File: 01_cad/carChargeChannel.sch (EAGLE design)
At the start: 100 parts, among them IC1 LT1513, IC3 PIC18F2420, T1 BC847A, T2 IRL530, X2 2X3

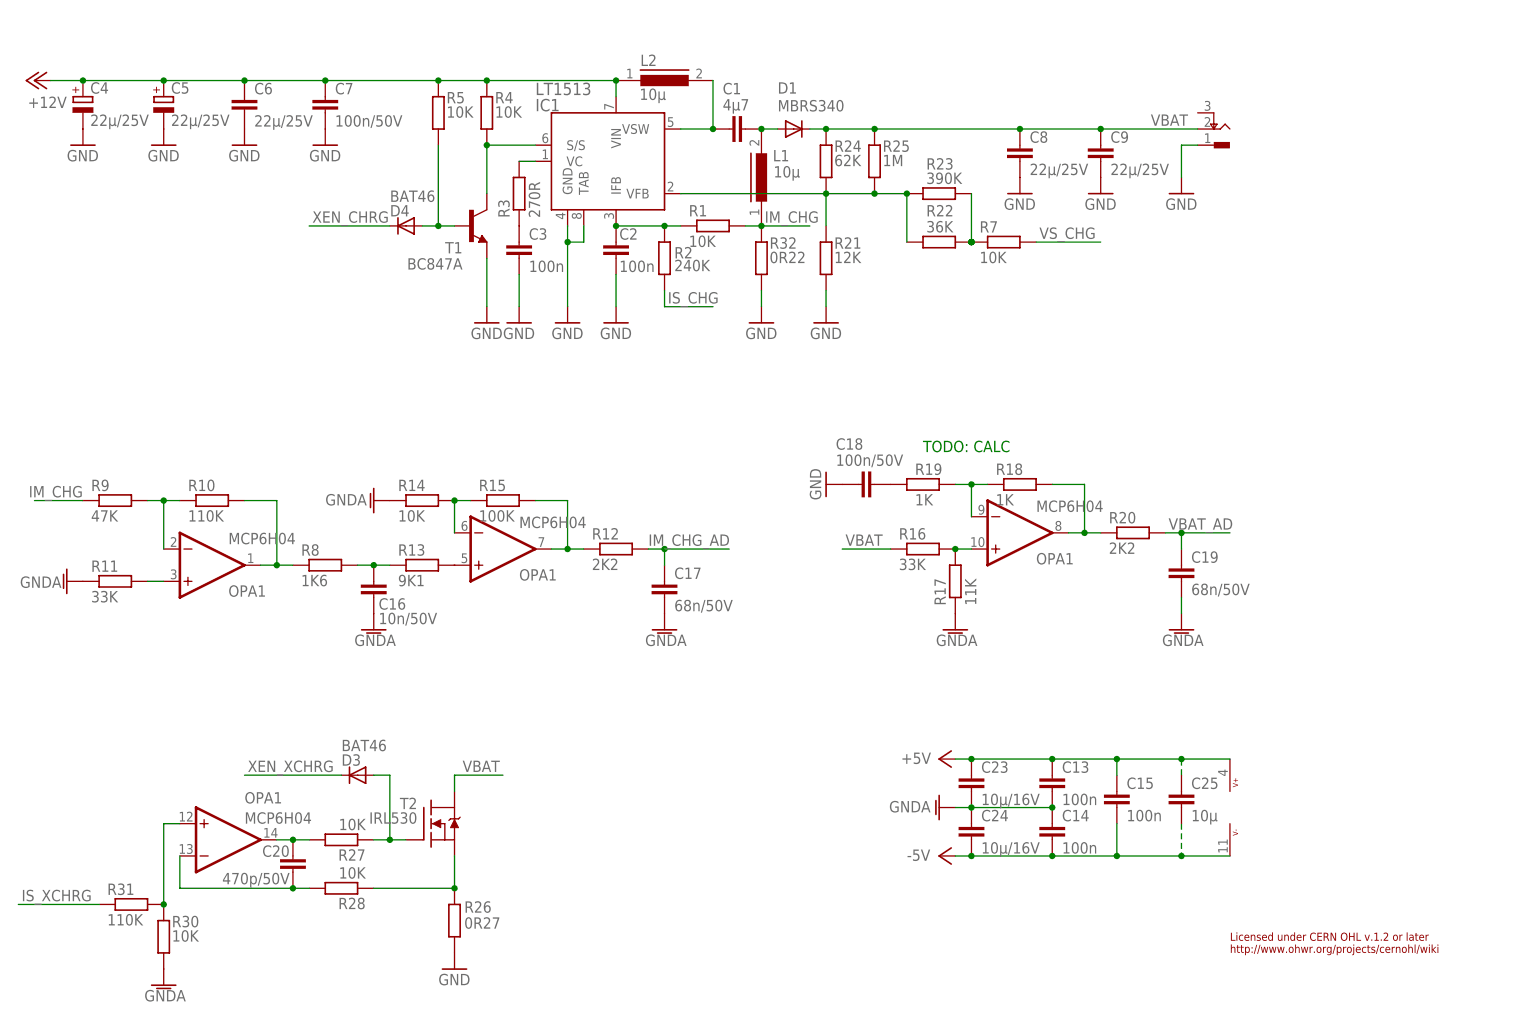
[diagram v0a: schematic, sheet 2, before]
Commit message: add TPS60403 for pwr supply
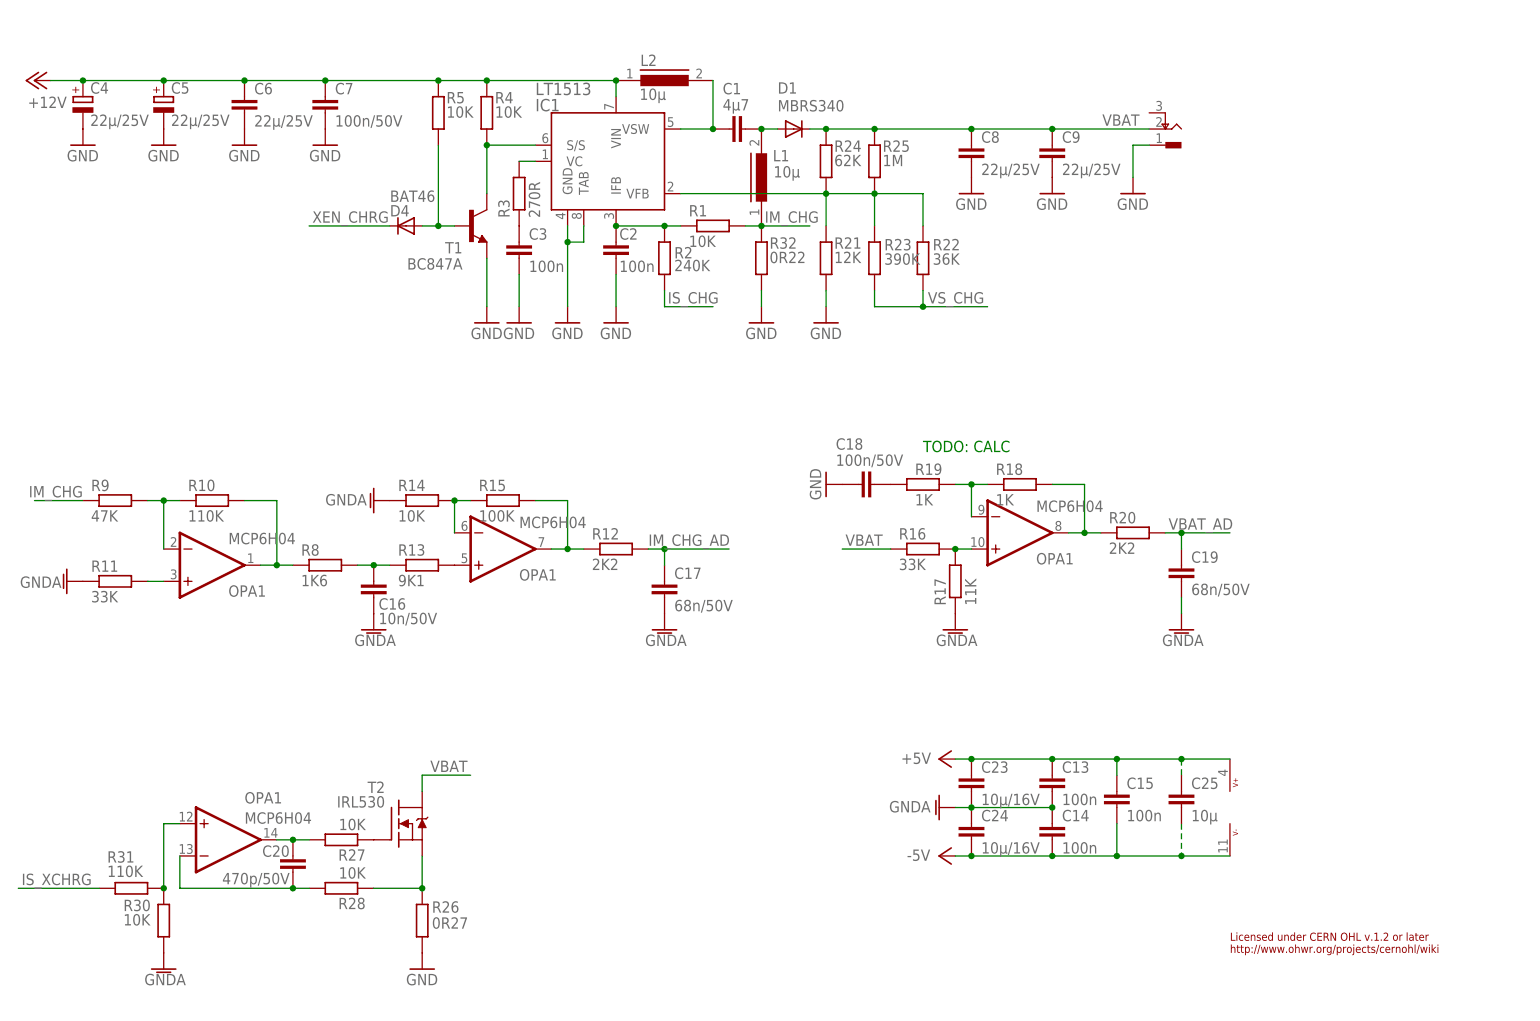
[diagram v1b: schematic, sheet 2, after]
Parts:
- removed D3: BAT46, omcDiode:BAT46W
- removed R7: 10K, omcResistor:R1206-10000-1%
- added IC2: PIC18F2420, omcPIC:PIC18F2420/SO
- IC3: value PIC18F2420 -> TPS60403; device omcPIC:PIC18F2420/SO -> omcPwrSupply:TPS60403DBVT
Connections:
- removed net LED1: IC3.5@RC
- removed net N$28: R22.1, R23.1, R7.1
- removed net XEN_XCHRG: D3.C, IC3.4@RB
- net !CS_DAC1: now also IC2.0@RB; no longer IC3.0@RB
- net !CS_DAC2: now also IC2.1@RB; no longer IC3.1@RB
- net !MCLR: now also IC2.!MCLR; no longer IC3.!MCLR
- net GND: now also IC2.VSS@VSS0, IC2.VSS@VSS1; no longer IC3.VSS@VSS0, IC3.VSS@VSS1
- net GNDA: now also IC2.4@RA; no longer IC3.4@RA
- net IM_CHG_AD: now also IC2.0@RA; no longer IC3.0@RA
- net LED2: now also IC2.5@RB; no longer IC3.5@RB
- net N$10: now also IC2.1@RC; no longer IC3.1@RC
- net N$20: now also IC2.0@RC; no longer IC3.0@RC
- net N$23: no longer D3.A
- net N$30: now also IC2.2@RC; no longer IC3.2@RC
- net N$34: now also IC2.OSC@1; no longer IC3.OSC@1
- net N$35: now also IC2.OSC@2; no longer IC3.OSC@2
- net PGC: now also IC2.6@RB; no longer IC3.6@RB
- net PGD: now also IC2.7@RB; no longer IC3.7@RB
- net PWRGD: now also IC2.2@RB; no longer IC3.2@RB
- net RXD: now also IC2.6@RC; no longer IC3.6@RC
- net SCL: now also IC2.3@RC; no longer IC3.3@RC
- net SDA: now also IC2.4@RC; no longer IC3.4@RC
- net TXD: now also IC2.7@RC; no longer IC3.7@RC
- net VBAT_AD: now also IC2.1@RA; no longer IC3.1@RA
- net VDD: now also IC2.VDD; no longer IC3.VDD
- net VREF_ADC: now also IC2.5@RA; no longer IC3.5@RA
- net VS_CHG: now also R22.1, R23.1; no longer R7.2
- net XEN_CHRG: now also IC2.3@RB; no longer IC3.3@RB
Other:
- note removed: "( 36k || 390k ) = 32.96k"
- moved on the sheet: C8, C9, R22, R23, R26, R30, R31, T2

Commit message: intermediate
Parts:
- removed C21, C36, C38, C39, C40: 47µ/6V, omcCapacitor:X5R-47000000P-1206
- removed C37, C41: 47µ/16V, omcCapacitor:X5R-47000000P-1210
- removed L3: 100µ, omcInductor:LQH3C101K
- removed R34: 0R, omcResistor:R1206-0.0-1%
- added C42, C43, C44: 1µ/50V, omcCapacitor:X7R-1000000P-1206
- added C45: 10µ/16V, omcCapacitor:X7R-10000000P-1206
- added C46: 47µ/16V, omcCapacitor:AEC-47U-16V-C
- added C47: 100n/50V, omcCapacitor:X7R-100000P-1206
- added C48: 22µ/16V, omcCapacitor:AEC-22U-16V-B
- added F1: T 1A0, omcFuse:OMT-T1A0-125V
- added IC4: 7805, omcPwrSupply:MC7805D2T
- added L5: 100µ, omcInductor:LQH3C101K
- added R7: 0R, omcResistor:R1206-0.0-1%
- C23, C24: value 10µ/16V -> 47µ/6V; device omcCapacitor:X7R-10000000P-1206 -> omcCapacitor:X5R-47000000P-1206
- C25: value 10µ -> 47µ/16V; device omcCapacitor:X7R-10000000P-1206 -> omcCapacitor:X5R-47000000P-1210
- C28: value 10µ -> 10µ/16V
- C31: value 10µ -> 47µ/16V; device omcCapacitor:X7R-10000000P-1206 -> omcCapacitor:AEC-47U-16V-C
- C4: value 22µ/25V -> 100n/50V; device omcCapacitor:AEC-22U-25V-C -> omcCapacitor:X7R-100000P-1206
- C5: value 22µ/25V -> 100µ/6V; device omcCapacitor:AEC-22U-25V-C -> omcCapacitor:X5R-100000000P-1206
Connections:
- net SCL renamed I2C_SCL
- net SDA renamed I2C_SDA
- removed net N$36: C36.2, C37.2, L4.1
- removed net PWRGD: IC2.2@RB
- new net LED1: IC2.4@RB
- new net N$22: C42.2, IC3.CFLY-
- new net N$28: C42.1, IC3.CFLY+
- new net N$33: C44.1, IC3.VO, L4.1
- new net N$40: F1.P$1
- net +12V: now also C28.1, C31.+, C4.1, C45.1, C46.+, C47.1, C48.+, F1.P$2, IC4.VI; no longer C4.+, C5.+
- net +5V: now also C24.1, L5.2; no longer C23.1, C28.1, C31.1, C39.1, C41.1, L3.2
- net -5V: now also C23.2; no longer C24.2, C40.2, C41.2
- net GND: now also C28.2, C31.-, C4.2, C43.2, C44.2, C45.2, C46.-, C47.2, C48.-, C5.2, IC3.GND, IC4.GND@1, R7.1; no longer C21.2, C36.1, C38.2, C4.-, C5.-, R34.2
- net GNDA: now also C23.1, C24.2, R7.2; no longer C23.2, C24.1, C28.2, C31.2, C39.2, C40.1, R34.1
- net VCC: now also C43.1, C5.1, IC3.VI, IC4.VO, L5.1; no longer C21.1, C37.1, C38.1, L3.1
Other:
- note removed: "DAC supply"
- moved on the sheet: C10, C11, C12, C22, C26, C27, C28, C29, C30, C32, C33, C34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

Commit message: intermediate
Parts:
- removed U$1: 24V/0A5, omcConnector:DC-PJ-SWT-5.7/2.5
- added C21: 68n/50V, omcCapacitor:X7R-68000P-1206
- added LED1: Green, omcOpto:LEDMONO-GREEN-KP3216
- added R29: 1K8, omcResistor:R1206-1800-1%
- added R34: 3K9, omcResistor:R1206-3900-1%
- added R35: 15K, omcResistor:R1206-15000-1%
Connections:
- net I2C_SCL renamed SCL
- net I2C_SDA renamed SDA
- new net N$36: LED1.A, R29.1
- new net VP12_AD: C21.1, IC2.2@RA, R34.2, R35.1
- net +12V: now also R35.2
- net +5V: now also R29.2
- net -5V: now also LED1.C
- net GND: no longer U$1G$2.P$1
- net GNDA: now also C21.2, R34.1
- net VBAT: no longer U$1G$1.P$1
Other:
- note added: "1 +"
- note added: "2"
- note added: "="
- note added: "= 19.4mV"
- note added: "DIG"
- note added: "LSB"
- note added: "NADC"
- note added: "PWR LED"
- note added: "R34"
- note added: "R35"
- note added: "VI"
- note added: "VREF"
- moved on the sheet: C29, C30, DAC1, DAC2

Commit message: intermediate
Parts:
- added D2: PMEG2010, omcDiode:PMEGXX10-20VBEA
- added JP1: (no value), pinhead:PINHD-1X3
- added R42, R43, R45, R46: 1K, omcResistor:R1206-1000-1%
- added R44: 47K, omcResistor:R1206-47000-1%
- added X3: DIN5, omcConnector:MAB-5S
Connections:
- new net EN_XCHRG: D2.C
- new net N$37: IC2.6@RC, R43.1
- new net N$38: IC2.7@RC, R42.1
- new net N$41: R45.1, X3G$4.P$1
- new net N$42: R46.1, X3G$5.P$1
- net GND: now also JP1.3, X3G$2.P$1, X3G$6.P$1, X3G$7.P$1
- net LED1: now also R45.2
- net LED2: now also R46.2
- net N$23: now also D2.A
- net RXD: now also JP1.1, R43.2, R44.1; no longer IC2.6@RC
- net TXD: now also JP1.2, R42.2; no longer IC2.7@RC
- net VBAT: now also X3G$1.P$1, X3G$3.P$1
- net VCC: now also R44.2
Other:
- note added: "RD1"
- note added: "RD2"
- note added: "Shield needs to be connectd with GND at plug"
- note added: "UART"
- note removed: "R34"
- note removed: "R35"
- moved on the sheet: C1, C10, C11, C12, C2, C21, C22, C23, C24, C25, C26, C27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

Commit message: intermediate4
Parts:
- added C36: 100n, omcCapacitor:X7R-100000P-1206
- added C37: 68n/50V, omcCapacitor:X7R-68000P-1206
- added D3: BAT46, omcDiode:BAT46W
- added R47, R48: 47K, omcResistor:R1206-47000-1%
- added R49: 15K, omcResistor:R1206-15000-1%
- added R50: 3K9, omcResistor:R1206-3900-1%
- added T3, T4: BSS138, omcTransistor:BSS138
- JP1: device pinhead:PINHD-1X3 -> pinhead:PINHD-1X4
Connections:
- removed net N$37: IC2.6@RC, R43.1
- removed net N$38: IC2.7@RC, R42.1
- new net +3V3: C36.1, JP1.1, R47.2, R48.2, T3.G, T4.G
- new net N$45: JP1.3, R48.1, T3.S
- new net N$46: JP1.2, R47.1, T4.S
- new net N$47: R42.1, T3.D
- new net N$48: R43.1, R44.1, T4.D
- new net VOPA_AD: C37.1, D3.C, IC2.3@RA, R49.1, R50.2
- net +5V: now also R49.2
- net -5V: now also R50.1
- net GND: now also C36.2, JP1.4; no longer JP1.3
- net GNDA: now also C37.2, D3.A
- net RXD: now also IC2.6@RC; no longer JP1.1, R44.1
- net TXD: now also IC2.7@RC; no longer JP1.2
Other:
- note added: "+3V3"
- note added: "GND"
- note added: "RXD"
- note added: "TXD"
- note added: "Voltage Level Translation"
- moved on the sheet: C21, LED1, R29, R34, R35, R42, R43, R44, X2

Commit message: intermediate
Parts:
- added H1, H2, H3, H4: D3.2, holes:MOUNT-PAD-ROUND3.2
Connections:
- net GND: now also H1.MOUNT, H2.MOUNT, H3.MOUNT, H4.MOUNT
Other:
- moved on the sheet: C13, C14, C15
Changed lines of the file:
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@@
 <part name="GND36" library="supply1" deviceset="GNDA" device=""/>
 <part name="P-3" library="supply1" deviceset="-5V" device=""/>
+<part name="H1" library="holes" deviceset="MOUNT-PAD-ROUND" device="3.2" value="D3.2"/>
+<part name="GND28" library="supply1" deviceset="GND" device=""/>
+<part name="H2" library="holes" deviceset="MOUNT-PAD-ROUND" device="3.2" value="D3.2"/>
+<part name="GND54" library="supply1" deviceset="GND" device=""/>
+<part name="H3" library="holes" deviceset="MOUNT-PAD-ROUND" device="3.2" value="D3.2"/>
+<part name="GND55" library="supply1" deviceset="GND" device=""/>
+<part name="H4" library="holes" deviceset="MOUNT-PAD-ROUND" device="3.2" value="D3.2"/>
+<part name="GND56" library="supply1" deviceset="GND" device=""/>
 </parts>
 <sheets>
@@
 <attribute name="VALUE" x="39.37" y="32.258" size="1.778" layer="96"/>
 </instance>
-<instance part="OPA1" gate="G$5" x="205.74" y="43.18"/>
-<instance part="C13" gate="G$1" x="187.96" y="48.26"/>
-<instance part="C14" gate="G$1" x="187.96" y="40.64"/>
-<instance part="C15" gate="G$1" x="198.12" y="45.72"/>
-<instance part="P+4" gate="1" x="180.34" y="50.8" smashed="yes" rot="R90">
-<attribute name="VALUE" x="179.07" y="51.816" size="1.778" layer="96" rot="R180"/>
-</instance>
-<instance part="P-2" gate="1" x="180.34" y="35.56" smashed="yes" rot="R270">
-<attribute name="VALUE" x="175.26" y="34.798" size="1.778" layer="96"/>
+<instance part="OPA1" gate="G$5" x="190.5" y="40.64"/>
+<instance part="C13" gate="G$1" x="172.72" y="45.72"/>
+<instance part="C14" gate="G$1" x="172.72" y="38.1"/>
+<instance part="C15" gate="G$1" x="182.88" y="43.18"/>
+<instance part="P+4" gate="1" x="165.1" y="48.26" smashed="yes" rot="R90">
+<attribute name="VALUE" x="163.83" y="49.276" size="1.778" layer="96" rot="R180"/>
+</instance>
+<instance part="P-2" gate="1" x="165.1" y="33.02" smashed="yes" rot="R270">
+<attribute name="VALUE" x="160.02" y="32.258" size="1.778" layer="96"/>
 </instance>
 <instance part="R26" gate="G$1" x="93.98" y="25.4" smashed="yes" rot="R90">
@@
 <attribute name="VALUE" x="72.39" y="129.54" size="1.778" layer="96" rot="R180"/>
 </instance>
-<instance part="GND15" gate="1" x="180.34" y="43.18" smashed="yes" rot="R270">
-<attribute name="VALUE" x="172.466" y="42.418" size="1.778" layer="96"/>
+<instance part="GND15" gate="1" x="165.1" y="40.64" smashed="yes" rot="R270">
+<attribute name="VALUE" x="157.226" y="39.878" size="1.778" layer="96"/>
 </instance>
 <instance part="P+13" gate="1" x="27.94" y="157.48" rot="R90"/>
@@
 <attribute name="VALUE" x="194.818" y="139.192" size="1.016" layer="96"/>
 </instance>
+<instance part="H1" gate="G$1" x="203.2" y="43.18" smashed="yes" rot="R90">
+<attribute name="NAME" x="205.994" y="43.7642" size="1.778" layer="95"/>
+<attribute name="VALUE" x="205.994" y="40.7162" size="1.778" layer="96"/>
+</instance>
+<instance part="GND28" gate="1" x="203.2" y="35.56"/>
+<instance part="H2" gate="G$1" x="215.9" y="43.18" smashed="yes" rot="R90">
+<attribute name="NAME" x="218.694" y="43.7642" size="1.778" layer="95"/>
+<attribute name="VALUE" x="218.694" y="40.7162" size="1.778" layer="96"/>
+</instance>
+<instance part="GND54" gate="1" x="215.9" y="35.56"/>
+<instance part="H3" gate="G$1" x="228.6" y="43.18" smashed="yes" rot="R90">
+<attribute name="NAME" x="231.394" y="43.7642" size="1.778" layer="95"/>
+<attribute name="VALUE" x="231.394" y="40.7162" size="1.778" layer="96"/>
+</instance>
+<instance part="GND55" gate="1" x="228.6" y="35.56"/>
+<instance part="H4" gate="G$1" x="241.3" y="43.18" smashed="yes" rot="R90">
+<attribute name="NAME" x="244.094" y="43.7642" size="1.778" layer="95"/>
+<attribute name="VALUE" x="244.094" y="40.7162" size="1.778" layer="96"/>
+</instance>
+<instance part="GND56" gate="1" x="241.3" y="35.56"/>
 </instances>
 <busses>
@@
 <pinref part="X3" gate="G$2" pin="P$1"/>
 <wire x1="203.2" y1="147.32" x2="205.74" y2="147.32" width="0.1524" layer="91"/>
+</segment>
+<segment>
+<pinref part="GND28" gate="1" pin="GND"/>
+<pinref part="H1" gate="G$1" pin="MOUNT"/>
+<wire x1="203.2" y1="38.1" x2="203.2" y2="40.64" width="0.1524" layer="91"/>
+</segment>
+<segment>
+<pinref part="GND54" gate="1" pin="GND"/>
+<pinref part="H2" gate="G$1" pin="MOUNT"/>
+<wire x1="215.9" y1="38.1" x2="215.9" y2="40.64" width="0.1524" layer="91"/>
+</segment>
+<segment>
+<pinref part="GND55" gate="1" pin="GND"/>
+<pinref part="H3" gate="G$1" pin="MOUNT"/>
+<wire x1="228.6" y1="38.1" x2="228.6" y2="40.64" width="0.1524" layer="91"/>
+</segment>
+<segment>
+<pinref part="GND56" gate="1" pin="GND"/>
+<pinref part="H4" gate="G$1" pin="MOUNT"/>
+<wire x1="241.3" y1="38.1" x2="241.3" y2="40.64" width="0.1524" layer="91"/>
 </segment>
 </net>
@@
 <pinref part="OPA1" gate="G$5" pin="V+"/>
 <pinref part="C13" gate="G$1" pin="1"/>
-<wire x1="205.74" y1="50.8" x2="198.12" y2="50.8" width="0.1524" layer="91"/>
-<wire x1="198.12" y1="50.8" x2="187.96" y2="50.8" width="0.1524" layer="91"/>
-<wire x1="187.96" y1="50.8" x2="182.88" y2="50.8" width="0.1524" layer="91"/>
-<junction x="187.96" y="50.8"/>
+<wire x1="190.5" y1="48.26" x2="182.88" y2="48.26" width="0.1524" layer="91"/>
+<wire x1="182.88" y1="48.26" x2="172.72" y2="48.26" width="0.1524" layer="91"/>
+<wire x1="172.72" y1="48.26" x2="167.64" y2="48.26" width="0.1524" layer="91"/>
+<junction x="172.72" y="48.26"/>
 <pinref part="P+4" gate="1" pin="+5V"/>
 <pinref part="C15" gate="G$1" pin="1"/>
-<wire x1="198.12" y1="48.26" x2="198.12" y2="50.8" width="0.1524" layer="91"/>
-<junction x="198.12" y="50.8"/>
+<wire x1="182.88" y1="45.72" x2="182.88" y2="48.26" width="0.1524" layer="91"/>
+<junction x="182.88" y="48.26"/>
 </segment>
 </net>
@@
 <pinref part="OPA1" gate="G$5" pin="V-"/>
 <pinref part="C14" gate="G$1" pin="2"/>
-<wire x1="205.74" y1="35.56" x2="198.12" y2="35.56" width="0.1524" layer="91"/>
-<wire x1="198.12" y1="35.56" x2="187.96" y2="35.56" width="0.1524" layer="91"/>
-<wire x1="187.96" y1="35.56" x2="182.88" y2="35.56" width="0.1524" layer="91"/>
-<junction x="187.96" y="35.56"/>
+<wire x1="190.5" y1="33.02" x2="182.88" y2="33.02" width="0.1524" layer="91"/>
+<wire x1="182.88" y1="33.02" x2="172.72" y2="33.02" width="0.1524" layer="91"/>
+<wire x1="172.72" y1="33.02" x2="167.64" y2="33.02" width="0.1524" layer="91"/>
+<junction x="172.72" y="33.02"/>
 <pinref part="P-2" gate="1" pin="-5V"/>
 <pinref part="C15" gate="G$1" pin="2"/>
-<wire x1="198.12" y1="40.64" x2="198.12" y2="35.56" width="0.1524" layer="91"/>
-<junction x="198.12" y="35.56"/>
+<wire x1="182.88" y1="38.1" x2="182.88" y2="33.02" width="0.1524" layer="91"/>
+<junction x="182.88" y="33.02"/>
 </segment>
 </net>
@@
 <pinref part="C14" gate="G$1" pin="1"/>
 <pinref part="C13" gate="G$1" pin="2"/>
-<junction x="187.96" y="43.18"/>
-<wire x1="182.88" y1="43.18" x2="187.96" y2="43.18" width="0.1524" layer="91"/>
+<junction x="172.72" y="40.64"/>
+<wire x1="167.64" y1="40.64" x2="172.72" y2="40.64" width="0.1524" layer="91"/>
 <pinref part="GND15" gate="1" pin="GNDA"/>
 </segment>

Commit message: ongoing...
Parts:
- added C38: 4µ7, omcCapacitor:X7R-4700000P-1206
- added C39: 100n/50V, omcCapacitor:X7R-100000P-1206
- C7: device omcCapacitor:X7R-100000P-0805 -> omcCapacitor:X7R-100000P-1206
- L1, L2: device omcInductor:PIS-10U-4720 -> omcInductor:DR-10U-74
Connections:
- net GND: now also C39.2
- net N$1: now also C38.2
- net N$2: now also C38.1
- net VBAT: now also C39.1
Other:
- moved on the sheet: R45, R46, X3

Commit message: intermediate
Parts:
- added C40: 47µ/16V, omcCapacitor:X5R-47000000P-1210
- added C41: 47µ/6V, omcCapacitor:X5R-47000000P-1206
- C28: value 10µ/16V -> 100n/50V; device omcCapacitor:X7R-10000000P-1206 -> omcCapacitor:X7R-100000P-1206
- C31: value 47µ/16V -> 47µ/6V; device omcCapacitor:AEC-47U-16V-C -> omcCapacitor:X5R-47000000P-1206
- C45: value 10µ/16V -> 47µ/16V; device omcCapacitor:X7R-10000000P-1206 -> omcCapacitor:X5R-47000000P-1210
- C5: value 100µ/6V -> 47µ/6V; device omcCapacitor:X5R-100000000P-1206 -> omcCapacitor:X5R-47000000P-1206
- D2: value PMEG2010 -> BAT46; device omcDiode:PMEGXX10-20VBEA -> omcDiode:BAT46W
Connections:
- net +12V: now also C40.1; no longer C31.+, C47.1
- net EN_XCHRG: now also IC2.2@RB
- net GND: now also C40.2, C41.2; no longer C31.-
- net VCC: now also C41.1, C47.1
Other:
- moved on the sheet: C28, C4, C43, C45, C46, C47, C48, C5, F1, IC4
